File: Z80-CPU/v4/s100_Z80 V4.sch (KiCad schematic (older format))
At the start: 144 parts, among them K1 CONN_3, K17 EN_WAITS, K2 CONN_3, P1 S100_MALE, P2 CONN_4X2, P3 CLK_CPU, P34 CONN_1, P35 CONN_1, P36 CONN_3X2, P4 CONN_2X2, P5 XILINX CABLE2, P6 MASTER_OSC, P7 NMI, P8 CPLD Pins, Q1 NPN, Q2 NPN, Q3 NPN, SW1 RESET, SW2 DIPS_08, SW3 DIPS_08, SW4 DIPS_08, U1 Z80, U10 74LS165, U11 74LS165, U12 ^^74LS541, U13 2732, U14 74LS682N, U15 74LS153, U16 74LS153, U17 XC9572XL-TQ100, U18 74LS32, U19 74LS244, U2 ^^74LS541, U20 74LS244, U21 ^^74LS541, U22 ^^74LS541, U23 74LS02, U24 74LS04, U25 74LS04, U26 ^^LOGO1, U27 74LS139, U28 74LS00, U29 74LS273, U3 ^^74LS541, U30 74LS273, U31 74LS00, U32 74LS273, U33 74LS74, U34 74LS74, U36 74LS04, U37 74LS05, U39 74LS273, U4 74LS04, U40 74LS00, U45 74LS02, U48 LDO_REG_7805, U5 74LS157, U6 74LS157, U7 74LS32, U8 74LS157, U9 74LS165

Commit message: Z80-CPU v4: schematic and placement
Source: S100 Z80 version4/backups/28-06-2015 1855 (the same folder also exists, byte-identical, in S100 Z80 version5/backups)
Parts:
- removed JP1: JUMPER, PIN_ARRAY_2X1, symbol JUMPER
- removed U17: XC9572XL-TQ100, ~, symbol XC9572XL-TQ100
- removed Ux1: ^^3.3VREG_SOT223, ~, symbol ^^3.3VREG_SOT223
- added C6: 0.1 uF, C2, symbol C
- added IC1: XC9572PC84, XILINX-PLCC-S84, symbol XC9572PC84
- added P9: CONN_2, ~, symbol CONN_2
- renumbered U24 to U25, U24 to U4
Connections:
- net labels added: CPLD_CLKin, CPLD_P19, CPLD_P44, CPLD_P46, CPLD_P47, CPLD_P51, CPLD_P52, CPLD_P54, CPLD_P55, CPLD_P62, CPLD_P63, CPLD_P66, CPLD_P72, CPLD_P80, CPLD_P81, CPLD_P84, CPLD_Pout1, CPLD_Pout10, CPLD_Pout2, CPLD_Pout3, CPLD_Pout4, CPLD_Pout5, CPLD_Pout6, CPLD_Pout7, CPLD_Pout8, CPLD_Pout9, V5.0temp
- net labels removed: CPLD_P10, CPLD_P12, CPLD_P22, CPLD_P27, CPLD_P42, CPLD_P49, CPLD_P78, CPLD_P8, CPLD_P87, CPLD_P9, CPLD_P91, CPLD_P93, CPLD_P94, CPLD_P95, CPLD_P96, CPLD_P97, CPLD_P99, V3.3b
- wire segments 1360 -> 1337
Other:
- note removed: "SOT233"
- moved on the sheet: Cx2

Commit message: Z80-CPU v4: schematic and placement
Source: S100 Z80 version4/backups/29-06-2015 1549 (the same folder also exists, byte-identical, in S100 Z80 version5/backups)
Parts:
- added C7: 0.1 uF, C2, symbol C
- added P10: CONN_2, ~, symbol CONN_2
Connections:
- wire segments 1337 -> 1346
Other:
- moved on the sheet: C54, P9
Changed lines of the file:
@@
 Sheet 1 1
 Title "noname.sch"
-Date "28 jun 2015"
+Date "29 jun 2015"
 Rev ""
 Comp ""
@@
 L C C54
 U 1 1 4BB69128
-P 32250 12900
+P 6600 18500
 AR Path="/4BB69128" Ref="C54"  Part="1"
 AR Path="/FFFFFFFF4BB69128" Ref="C54"  Part="1"
@@
 AR Path="/69549BC04BB69128" Ref="C54"  Part="1"
 AR Path="/D1C3384BB69128" Ref="C54"  Part="1"
-F 0 "C54" H 32300 13000 50  0000 L CNN
-F 1 "0.1 uF" H 32300 12800 50  0000 L CNN
-F 2 "C2" H 32250 12900 60  0001 C CNN
-F 3 "" H 32250 12900 60  0001 C CNN
-	1    32250 12900
+F 0 "C54" H 6650 18600 50  0000 L CNN
+F 1 "0.1 uF" H 6650 18400 50  0000 L CNN
+F 2 "C2" H 6600 18500 60  0001 C CNN
+F 3 "" H 6600 18500 60  0001 C CNN
+	1    6600 18500
 	1    0    0    -1
 $EndComp
@@
 	1    0    0    -1
 $EndComp
-Text Label 5650 18100 0    60   ~ 0
+Text Label 7000 17650 0    60   ~ 0
 V5.0
 Text Label 5900 19600 0    60   ~ 0
@@
 L CONN_2 P9
 U 1 1 55944619
-P 6100 18350
-F 0 "P9" V 6050 18350 40  0000 C CNN
-F 1 "CONN_2" V 6150 18350 40  0000 C CNN
-F 2 "~" H 6100 18350 60  0000 C CNN
-F 3 "~" H 6100 18350 60  0000 C CNN
-	1    6100 18350
+P 7450 17900
+F 0 "P9" V 7400 17900 40  0000 C CNN
+F 1 "CONN_2" V 7500 17900 40  0000 C CNN
+F 2 "~" H 7450 17900 60  0000 C CNN
+F 3 "~" H 7450 17900 60  0000 C CNN
+	1    7450 17900
 	1    0    0    -1
 $EndComp
 Wire Wire Line
-	5650 18100 5650 18250
+	7000 17650 7000 17800
 Wire Wire Line
-	5650 18250 5750 18250
+	7000 17800 7100 17800
 Text Label 5650 18650 0    60   ~ 0
 V5.0temp
 Wire Wire Line
-	5750 18450 5400 18450
+	6300 18450 5400 18450
 Wire Wire Line
 	5650 18650 5550 18650
@@
 	5550 18650 5550 18450
 Connection ~ 5550 18450
+$Comp
+L C C7
+U 1 1 559463A1
+P 6900 18500
+F 0 "C7" H 6950 18600 50  0000 L CNN
+F 1 "0.1 uF" H 6950 18400 50  0000 L CNN
+F 2 "C2" H 6900 18500 60  0001 C CNN
+F 3 "" H 6900 18500 60  0001 C CNN
+	1    6900 18500
+	1    0    0    -1
+$EndComp
+Wire Wire Line
+	6300 17800 6300 18450
+Wire Wire Line
+	6300 18000 7100 18000
+Wire Wire Line
+	6900 18300 6900 18000
+Connection ~ 6900 18000
+Wire Wire Line
+	6600 18300 6600 18000
+Connection ~ 6600 18000
+Text Label 7000 18850 0    60   ~ 0
+GND
+Wire Wire Line
+	6600 18700 6600 18850
+Wire Wire Line
+	6600 18850 7000 18850
+Wire Wire Line
+	6900 18700 6900 18850
+Connection ~ 6900 18850
+$Comp
+L CONN_2 P10
+U 1 1 55949444
+P 6650 17700
+F 0 "P10" V 6600 17700 40  0000 C CNN
+F 1 "CONN_2" V 6700 17700 40  0000 C CNN
+F 2 "~" H 6650 17700 60  0000 C CNN
+F 3 "~" H 6650 17700 60  0000 C CNN
+	1    6650 17700
+	1    0    0    -1
+$EndComp
+Text Label 6250 17450 0    60   ~ 0
+V5.0
+Connection ~ 6300 18000
+Wire Wire Line
+	6250 17450 6250 17600
+Wire Wire Line
+	6250 17600 6300 17600
 $EndSCHEMATC

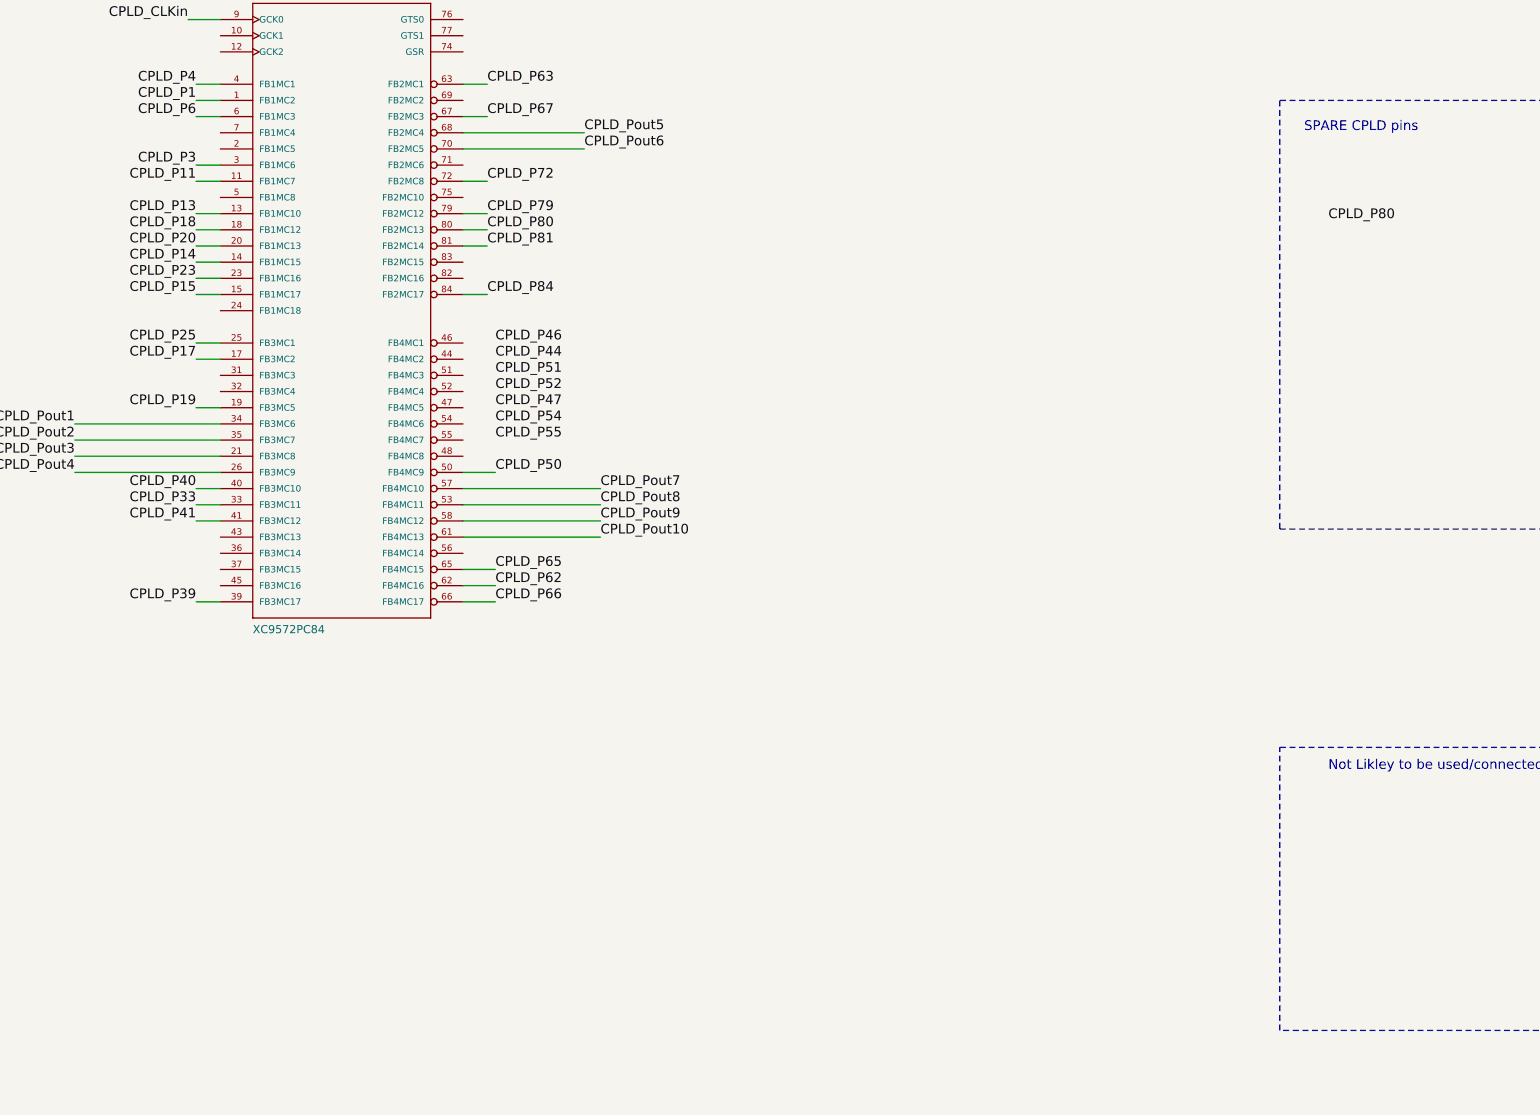
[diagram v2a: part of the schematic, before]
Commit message: Z80-CPU v4: schematic and routed trial
Source: S100 Z80 version4/backups/30-06-2015 morning (the same folder also exists, byte-identical, in S100 Z80 version5/backups)
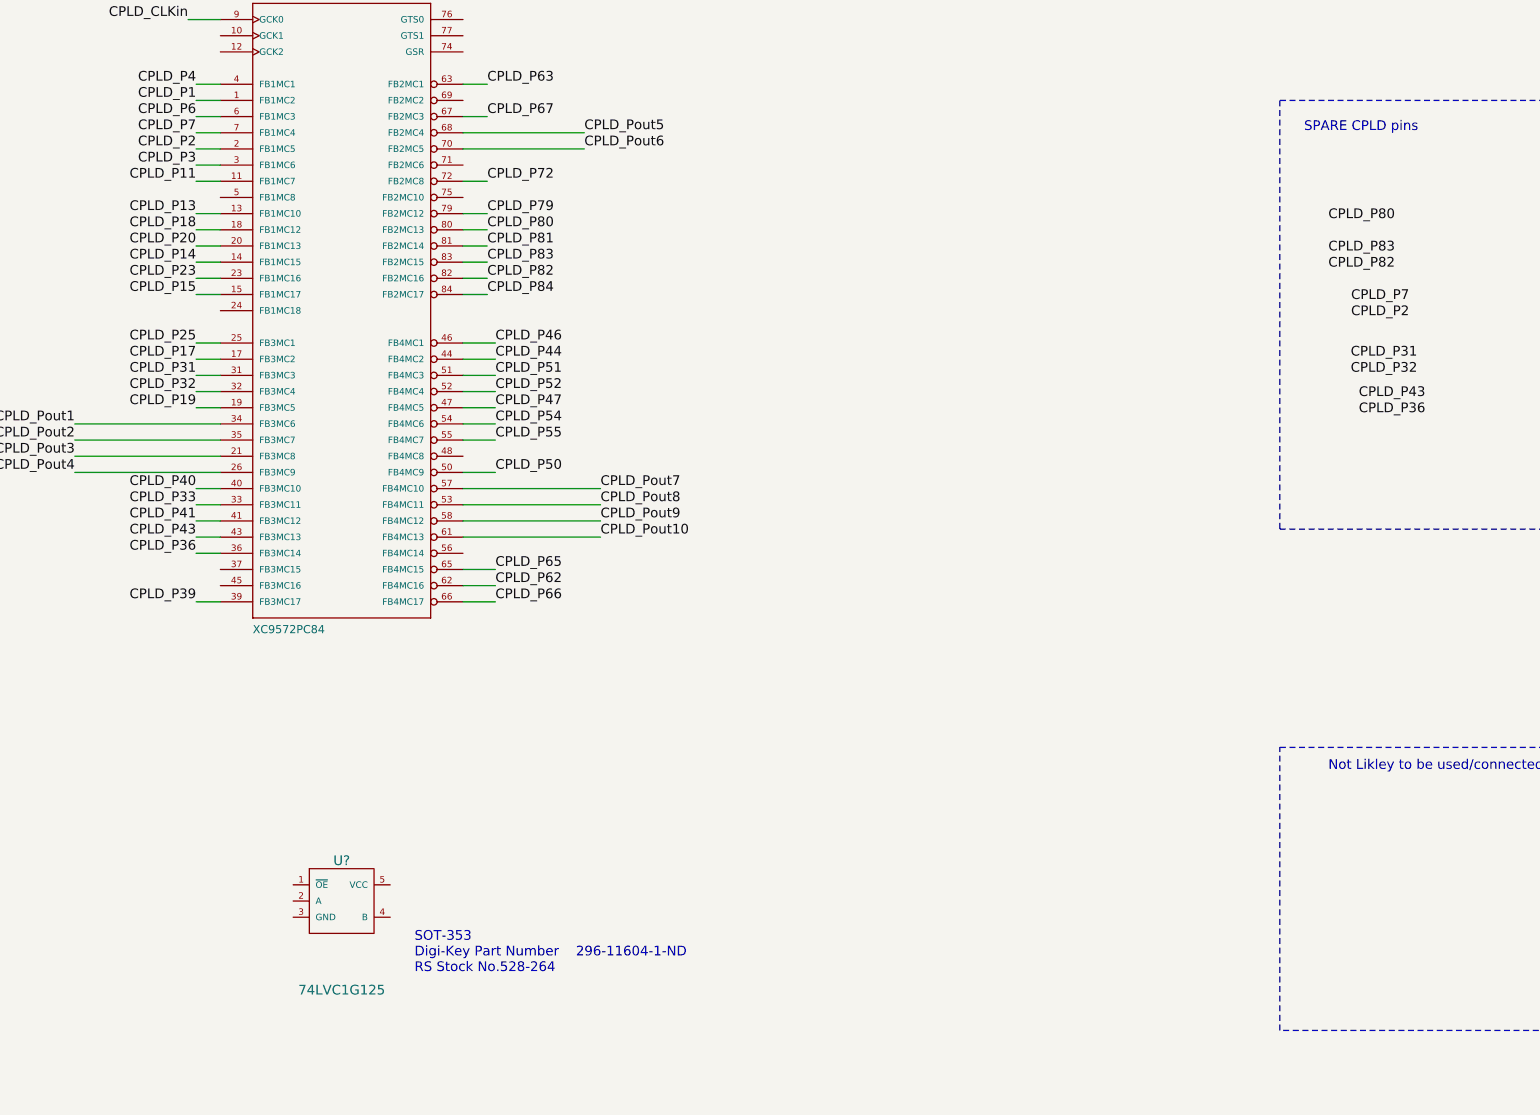
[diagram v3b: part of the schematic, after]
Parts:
- added U?: 74LVC1G125, symbol 74LVC1G125
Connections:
- net labels added: CPLD_P2, CPLD_P31, CPLD_P32, CPLD_P36, CPLD_P43, CPLD_P7, CPLD_P82, CPLD_P83
- wire segments 1346 -> 1361
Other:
- note added: "SOT-353\nDigi-Key Part Number 296-11604-1-ND\nRS Stock No.528-264"
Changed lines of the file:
@@
 Wire Wire Line
 	6250 17600 6300 17600
+$Comp
+L 74LVC1G125 U?
+U 1 1 5594B4D5
+P 5650 26600
+F 0 "U?" H 5650 26600 60  0000 C CNN
+F 1 "74LVC1G125" H 5650 25800 60  0000 C CNN
+F 2 "" H 5650 26600 60  0000 C CNN
+F 3 "" H 5650 26600 60  0000 C CNN
+	1    5650 26600
+	1    0    0    -1
+$EndComp
+Text Notes 6100 27300 0    60   ~ 0
+SOT-353\nDigi-Key Part Number	296-11604-1-ND\nRS Stock No.528-264
+Text Label 6550 22900 0    60   ~ 0
+CPLD_P83
+Text Label 6550 23000 0    60   ~ 0
+CPLD_P82
+Text Label 11750 22850 0    60   ~ 0
+CPLD_P83
+Text Label 11750 22950 0    60   ~ 0
+CPLD_P82
+Wire Wire Line
+	6550 22900 6400 22900
+Wire Wire Line
+	6400 23000 6550 23000
+Wire Wire Line
+	4900 22100 4750 22100
+Wire Wire Line
+	4900 22200 4750 22200
+Text Label 4750 22100 2    60   ~ 0
+CPLD_P7
+Text Label 4750 22200 2    60   ~ 0
+CPLD_P2
+Text Label 12250 23150 2    60   ~ 0
+CPLD_P7
+Text Label 12250 23250 2    60   ~ 0
+CPLD_P2
+Text Label 4750 23600 2    60   ~ 0
+CPLD_P31
+Text Label 4750 23700 2    60   ~ 0
+CPLD_P32
+Text Label 12300 23500 2    60   ~ 0
+CPLD_P31
+Text Label 12300 23600 2    60   ~ 0
+CPLD_P32
+Wire Wire Line
+	4750 23600 4900 23600
+Wire Wire Line
+	4900 23700 4750 23700
+Text Label 4750 24600 2    60   ~ 0
+CPLD_P43
+Text Label 4750 24700 2    60   ~ 0
+CPLD_P36
+Wire Wire Line
+	4900 24600 4750 24600
+Wire Wire Line
+	4750 24700 4900 24700
+Text Label 12350 23750 2    60   ~ 0
+CPLD_P43
+Text Label 12350 23850 2    60   ~ 0
+CPLD_P36
+Wire Wire Line
+	6600 23400 6400 23400
+Wire Wire Line
+	6400 23500 6600 23500
+Wire Wire Line
+	6600 23600 6400 23600
+Wire Wire Line
+	6400 23700 6600 23700
+Wire Wire Line
+	6600 23800 6400 23800
+Wire Wire Line
+	6400 23900 6600 23900
+Wire Wire Line
+	6600 24000 6400 24000
 $EndSCHEMATC

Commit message: Z80-CPU v4: schematic, netlist and placement
Source: S100 Z80 version4/backups/30-06-2015 1801 (the same folder also exists, byte-identical, in S100 Z80 version5/backups)
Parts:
- removed P8: CPLD Pins, symbol CONN_5X2
- added P8: CPLD Pins, symbol CONN_6X2
- gave numbers to parts that had none: 1
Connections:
- net labels added: CPLD_P71, CPLD_P74, CPLD_P75, CPLD_P76, CPLD_P77
- wire segments 1361 -> 1386
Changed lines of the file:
@@
 Wire Wire Line
 	40800 2550 40950 2550
-Text Label 18950 22900 0    60   ~ 0
+Text Label 5750 28100 2    60   ~ 0
 CPLD_P33
 $Comp
@@
 Wire Wire Line
 	12400 19000 12400 20200
-$Comp
-L CONN_5X2 P8
-U 1 1 5592EEE1
-P 12050 18150
-F 0 "P8" H 12050 18450 60  0000 C CNN
-F 1 "CPLD Pins" V 12050 18150 50  0000 C CNN
-F 2 "" H 12050 18150 60  0000 C CNN
-F 3 "" H 12050 18150 60  0000 C CNN
-	1    12050 18150
-	1    0    0    -1
-$EndComp
 Wire Wire Line
 	11650 17950 11200 17950
@@
 Text Label 40800 3450 2    60   ~ 0
 CPLD_P81
-Text Label 11750 22650 0    60   ~ 0
+Text Label 5750 28300 2    60   ~ 0
 CPLD_P80
 Wire Wire Line
@@
 	6250 17600 6300 17600
 $Comp
-L 74LVC1G125 U?
+L 74LVC1G125 U17
 U 1 1 5594B4D5
 P 5650 26600
-F 0 "U?" H 5650 26600 60  0000 C CNN
+F 0 "U17" H 5650 26600 60  0000 C CNN
 F 1 "74LVC1G125" H 5650 25800 60  0000 C CNN
 F 2 "" H 5650 26600 60  0000 C CNN
@@
 Text Label 6550 23000 0    60   ~ 0
 CPLD_P82
-Text Label 11750 22850 0    60   ~ 0
+Text Label 5750 28400 2    60   ~ 0
 CPLD_P83
-Text Label 11750 22950 0    60   ~ 0
+Text Label 5750 28500 2    60   ~ 0
 CPLD_P82
 Wire Wire Line
@@
 Text Label 4750 22200 2    60   ~ 0
 CPLD_P2
-Text Label 12250 23150 2    60   ~ 0
+Text Label 5750 28600 2    60   ~ 0
 CPLD_P7
-Text Label 12250 23250 2    60   ~ 0
+Text Label 5750 28700 2    60   ~ 0
 CPLD_P2
 Text Label 4750 23600 2    60   ~ 0
@@
 Text Label 4750 23700 2    60   ~ 0
 CPLD_P32
-Text Label 12300 23500 2    60   ~ 0
+Text Label 5200 26850 2    60   ~ 0
 CPLD_P31
-Text Label 12300 23600 2    60   ~ 0
+Text Label 5200 26750 2    60   ~ 0
 CPLD_P32
 Wire Wire Line
@@
 Wire Wire Line
 	4750 24700 4900 24700
-Text Label 12350 23750 2    60   ~ 0
+Text Label 5750 28800 2    60   ~ 0
 CPLD_P43
-Text Label 12350 23850 2    60   ~ 0
+Text Label 5750 28900 2    60   ~ 0
 CPLD_P36
 Wire Wire Line
@@
 Wire Wire Line
 	6600 24000 6400 24000
+$Comp
+L CONN_6X2 P8
+U 1 1 559529E8
+P 12050 18200
+F 0 "P8" H 12050 18550 60  0000 C CNN
+F 1 "CPLD Pins" V 12050 18200 60  0000 C CNN
+F 2 "" H 12050 18200 60  0000 C CNN
+F 3 "" H 12050 18200 60  0000 C CNN
+	1    12050 18200
+	1    0    0    -1
+$EndComp
+Text Label 6550 22300 0    60   ~ 0
+CPLD_P71
+Text Label 6550 22500 0    60   ~ 0
+CPLD_P75
+Text Label 5750 29000 2    60   ~ 0
+CPLD_P71
+Text Label 12450 22700 0    60   ~ 0
+CPLD_P75
+Wire Wire Line
+	6550 22300 6400 22300
+Wire Wire Line
+	6400 22500 6550 22500
+Text Label 6550 21400 0    60   ~ 0
+CPLD_P76
+Text Label 6550 21500 0    60   ~ 0
+CPLD_P77
+Text Label 6550 21600 0    60   ~ 0
+CPLD_P74
+Wire Wire Line
+	6550 21400 6400 21400
+Wire Wire Line
+	6400 21500 6550 21500
+Wire Wire Line
+	6550 21600 6400 21600
+Text Label 18950 22900 0    60   ~ 0
+CPLD_P76
+Text Label 13200 18600 0    60   ~ 0
+CPLD_P77
+Text Label 13200 18700 0    60   ~ 0
+CPLD_P74
+Text Label 6100 26750 0    60   ~ 0
+V5.0
+Text Label 5200 26950 2    60   ~ 0
+GND
+Wire Wire Line
+	6100 26750 5950 26750
+Wire Wire Line
+	5350 26950 5200 26950
+Text Label 6100 26950 0    60   ~ 0
+D0
+Wire Wire Line
+	5950 26950 6100 26950
+Wire Wire Line
+	5350 26750 5200 26750
+Wire Wire Line
+	5200 26850 5350 26850
+Text Label 6050 29000 0    60   ~ 0
+bA7
+Text Label 6050 28900 0    60   ~ 0
+bA6
+Text Label 6050 28800 0    60   ~ 0
+bA5
+Text Label 6050 28700 0    60   ~ 0
+bA4
+Text Label 6050 28600 0    60   ~ 0
+bA3
+Text Label 6050 28500 0    60   ~ 0
+bA2
+Text Label 6050 28400 0    60   ~ 0
+bA1
+Text Label 6050 28300 0    60   ~ 0
+bA0
+Text Label 6050 28100 0    60   ~ 0
+D0
+Wire Wire Line
+	5750 28100 6050 28100
+Wire Wire Line
+	6050 28300 5750 28300
+Wire Wire Line
+	5750 28400 6050 28400
+Wire Wire Line
+	6050 28500 5750 28500
+Wire Wire Line
+	5750 28600 6050 28600
+Wire Wire Line
+	5750 28700 6050 28700
+Wire Wire Line
+	6050 28800 5750 28800
+Wire Wire Line
+	5750 28900 6050 28900
+Wire Wire Line
+	6050 29000 5750 29000
+Wire Wire Line
+	12450 18450 12950 18450
+Wire Wire Line
+	12950 18450 12950 18600
+Wire Wire Line
+	12950 18600 13200 18600
+Wire Wire Line
+	11650 18450 11550 18450
+Wire Wire Line
+	11550 18450 11550 18700
+Wire Wire Line
+	11550 18700 13200 18700
 $EndSCHEMATC

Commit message: Z80-CPU v4: schematic, placement and IC parts list
Source: S100 Z80 version4/backups/02-07-215 1901 (the same folder also exists, byte-identical, in S100 Z80 version5/backups) (folder name has a year typo: 215).
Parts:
- added P11: CONN_6, symbol CONN_6
- added unit 4 of U25
- added unit 5 of U25
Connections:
- net labels added: CPLD_P48, CPLD_P69
- net labels removed: CLK, CPLD_P16, READ_STROBE
- wire segments 1386 -> 1396
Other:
- note added: "A0 input"
- note added: "A1 input"
- note added: "A2 input"
- note added: "A3 input"
- note added: "A4 input"
- note added: "A5 input"
- note added: "A6 input"
- note added: "A7 input"
- note added: "CLK - input"
- note added: "Clave clear button - input"
- note added: "Clave clear from CPLD - output"
- note added: "D0 input"
- note added: "IORQ* input"
- note added: "IORQ+ output"
- note added: "LED D10 output"
- note added: "LED D4 output"
- note added: "LED D5 output"
- note added: "LED D6 output"
- note added: "LED D7 output"
- note added: "LED D9 output"
- note added: "M1* input"
- note added: "M1+ output"
- note added: "MREQ* input"
- note added: "MREQ+ output"
- note added: "MWRTb output"
- note added: "P11_2 I/O"
- note added: "P11_3 I/O"
- note added: "P11_4 I/O"
- note added: "P11_5 I/O"
- note added: "P11_6 I/O"
- note added: "P8_1 I/O"
- note added: "P8_10 I/O"
- note added: "P8_11 I/O"
- note added: "P8_2 I/O"
- note added: "P8_3 I/O"
- note added: "P8_4 I/O"
- note added: "P8_5 I/O"
- note added: "P8_6 I/O"
- note added: "P8_7 I/O"
- note added: "P8_8 I/O"
- note added: "P8_9 I/O"
- note added: "PortD0 bit7 input"
- note added: "PortD1 bit7 input"
- note added: "RD* input"
- note added: "RD+ output"
- note added: "REFSH* input"
- note added: "RESET*b - input"
- note added: "SLAVE_CLR* input to CPLD from S100 Bus"
- note added: "SLAVE_CLR* input to CPLD\nfrom S100 Bus"
- note added: "U17 A output"
- note added: "U17 OE output"
- note added: "WAIT+ input"
- note added: "WR* input"
- note added: "WR+ output"
- note added: "from S100 bus"
- note added: "pSTVAL* - output"
- note added: "pSYNCb - output"
- note added: "pWR*b - output"
- note added: "partial latch - output"
- note added: "sINPb - output"
- note added: "sINTAb - output"
- note added: "sMEMRb - output"
- note added: "sOUTb - output"
- note added: "sWO*b - output"
- note added: "to CPU and other devices on board"
